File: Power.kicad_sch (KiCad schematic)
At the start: 24 parts, among them J5 Conn_01x01_Pin, J6 Conn_01x01_Pin, U11 LMP8640, U12 LMV324, U2 LM2776, U6 LM1117MP-3.3, U7 LM337L_SO8

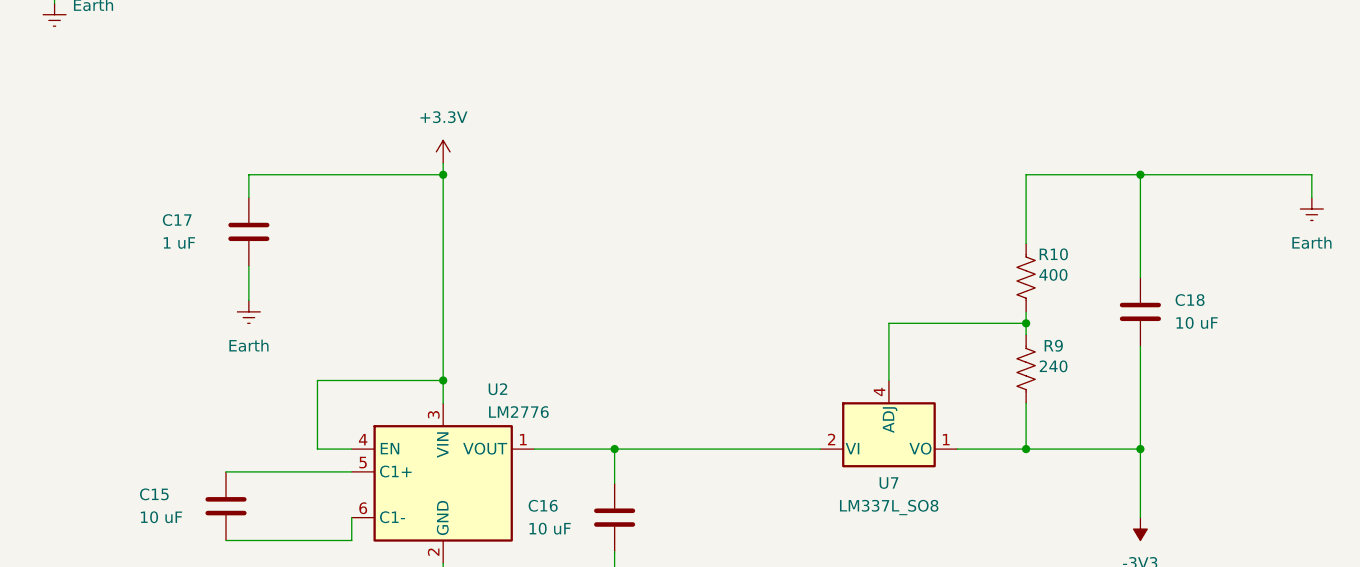
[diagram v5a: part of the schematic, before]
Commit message: changed schematics
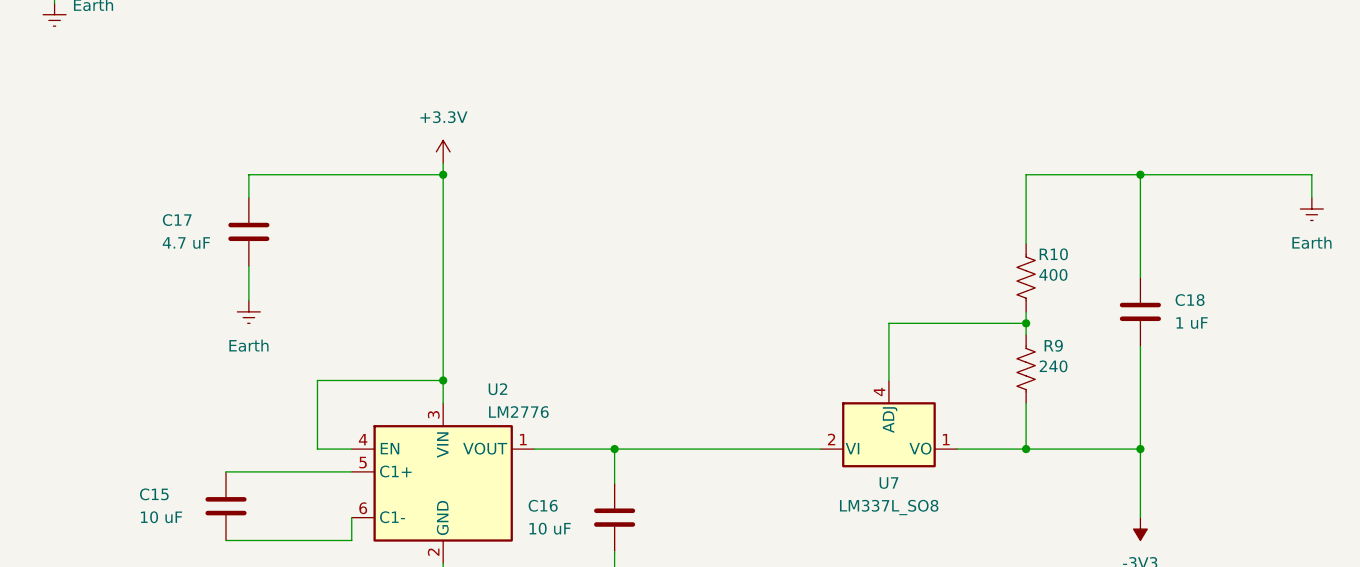
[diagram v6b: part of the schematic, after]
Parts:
- C17: value 1 uF -> 4.7 uF
- C18: value 10 uF -> 1 uF
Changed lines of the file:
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@@
 			)
 		)
-		(property "Value" "10 uF"
+		(property "Value" "1 uF"
 			(at 260.35 96.5199 0)
 			(effects
@@
 			)
 		)
-		(property "Value" "1 uF"
+		(property "Value" "4.7 uF"
 			(at 147.828 87.63 0)
 			(effects

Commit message: changes to schematic
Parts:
- C15: value 10 uF -> 1 uF
- C16: value 10 uF -> 4.7 uF
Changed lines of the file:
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@@
 			)
 		)
-		(property "Value" "10 uF"
+		(property "Value" "1 uF"
 			(at 145.288 118.11 0)
 			(effects
@@
 			)
 		)
-		(property "Value" "10 uF"
+		(property "Value" "4.7 uF"
 			(at 188.468 119.38 0)
 			(effects
